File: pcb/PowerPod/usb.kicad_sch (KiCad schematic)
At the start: 8 parts, among them IC2 FUSB302MPX, J1 GT-USB-7010, U1 SRV05-4

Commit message: finished layout
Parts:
- added C14, C24, C25: 100n, Capacitor_SMD:C_0402_1005Metric, symbol Capacitor_JLC:100n
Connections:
- net +3V3: now also C14.2, C24.2, C25.2
- net GND: now also C14.1, C24.1, C25.1
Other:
- moved on the sheet: C6

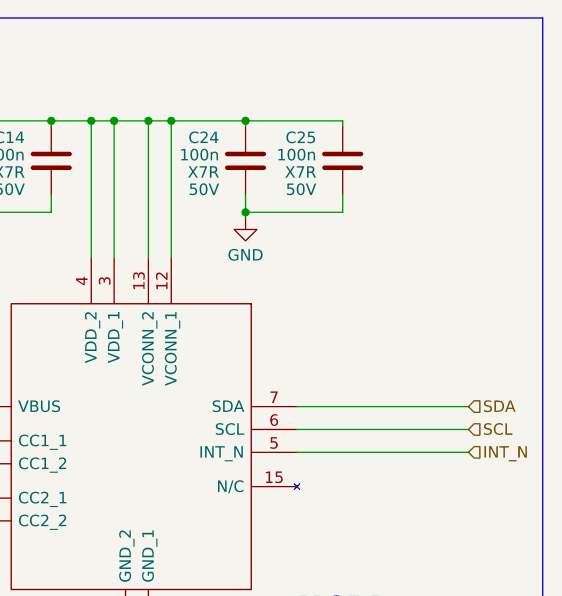
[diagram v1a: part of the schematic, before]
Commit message: changed gpio pins
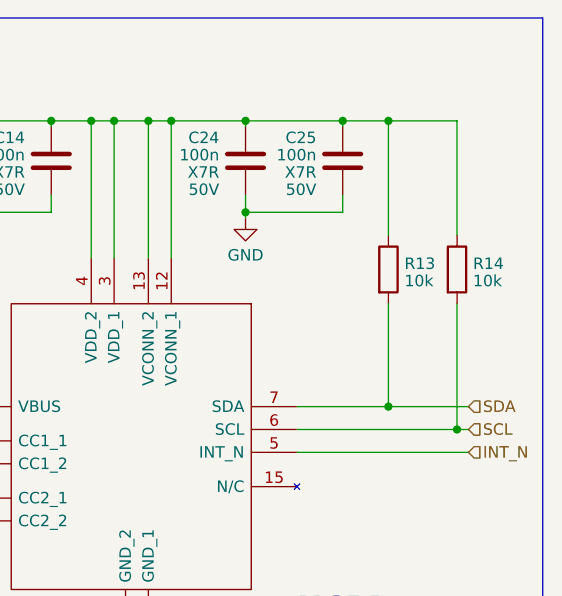
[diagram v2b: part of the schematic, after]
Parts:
- added R13, R14: 10k, Resistor_SMD:R_0402_1005Metric, symbol Resistor_JLC:10k
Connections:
- net +3V3: now also R13.1, R14.1
- net SCL: now also R14.2
- net SDA: now also R13.2
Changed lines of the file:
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@@
   (junction (at 279.4 71.12) (diameter 0) (color 0 0 0 0)
   )
+  (junction (at 335.28 105.41) (diameter 0) (color 0 0 0 0)
+  )
   (junction (at 167.005 102.87) (diameter 0) (color 0 0 0 0)
   )
@@
   (junction (at 126.365 174.625) (diameter 0) (color 0 0 0 0)
   )
+  (junction (at 327.66 102.87) (diameter 0) (color 0 0 0 0)
+  )
   (junction (at 146.685 153.035) (diameter 0) (color 0 0 0 0)
   )
   (junction (at 294.64 71.12) (diameter 0) (color 0 0 0 0)
   )
+  (junction (at 322.58 71.12) (diameter 0) (color 0 0 0 0)
+  )
   (junction (at 256.54 180.34) (diameter 0) (color 0 0 0 0)
+  )
+  (junction (at 327.66 71.12) (diameter 0) (color 0 0 0 0)
   )
   (junction (at 303.53 71.12) (diameter 0) (color 0 0 0 0)
@@
   (no_connect (at 144.145 163.195))
   (no_connect (at 144.145 165.735))
+  (wire (pts (xy 327.66 102.87) (xy 336.55 102.87))
+    (stroke (width 0) (type default))
+  )
   (wire (pts (xy 167.005 102.87) (xy 167.005 137.795))
     (stroke (width 0) (type default))
@@
     (stroke (width 0) (type default))
   )
+  (wire (pts (xy 335.28 71.12) (xy 335.28 83.82))
+    (stroke (width 0) (type default))
+  )
   (wire (pts (xy 182.88 140.335) (xy 182.88 142.875))
     (stroke (width 0) (type default))
@@
     (stroke (width 0) (type default))
   )
+  (wire (pts (xy 335.28 91.44) (xy 335.28 105.41))
+    (stroke (width 0) (type default))
+  )
   (wire (pts (xy 290.195 71.12) (xy 294.64 71.12))
     (stroke (width 0) (type default))
@@
     (stroke (width 0) (type default))
   )
+  (wire (pts (xy 327.66 91.44) (xy 327.66 102.87))
+    (stroke (width 0) (type default))
+  )
   (wire (pts (xy 197.485 135.255) (xy 227.965 135.255))
     (stroke (width 0) (type default))
@@
     (stroke (width 0) (type default))
   )
+  (wire (pts (xy 335.28 105.41) (xy 336.55 105.41))
+    (stroke (width 0) (type default))
+  )
   (wire (pts (xy 300.99 130.81) (xy 300.99 132.715))
     (stroke (width 0) (type default))
@@
     (stroke (width 0) (type default))
   )
-  (wire (pts (xy 317.5 105.41) (xy 336.55 105.41))
+  (wire (pts (xy 317.5 105.41) (xy 335.28 105.41))
     (stroke (width 0) (type default))
   )
@@
     (stroke (width 0) (type default))
   )
+  (wire (pts (xy 327.66 71.12) (xy 327.66 83.82))
+    (stroke (width 0) (type default))
+  )
   (wire (pts (xy 121.285 175.895) (xy 126.365 175.895))
     (stroke (width 0) (type default))
@@
     (stroke (width 0) (type default))
   )
-  (wire (pts (xy 317.5 102.87) (xy 336.55 102.87))
+  (wire (pts (xy 317.5 102.87) (xy 327.66 102.87))
     (stroke (width 0) (type default))
   )
@@
     (stroke (width 0) (type default))
   )
+  (wire (pts (xy 322.58 71.12) (xy 327.66 71.12))
+    (stroke (width 0) (type default))
+  )
   (wire (pts (xy 126.365 173.355) (xy 126.365 174.625))
+    (stroke (width 0) (type default))
+  )
+  (wire (pts (xy 327.66 71.12) (xy 335.28 71.12))
     (stroke (width 0) (type default))
   )
@@
     )
   )
+  (symbol (lib_id "Resistor_JLC:10k") (at 327.66 87.63 0) (unit 1)
+    (in_bom yes) (on_board yes) (dnp no) (fields_autoplaced)
+    (property "Reference" "R13" (at 329.438 86.9863 0)
+      (effects (font (size 1.27 1.27)) (justify left))
+    )
+    (property "Value" "10k" (at 329.438 88.9073 0)
+      (effects (font (size 1.27 1.27)) (justify left))
+    )
+    (property "Footprint" "Resistor_SMD:R_0402_1005Metric" (at 325.882 87.63 90)
+      (effects (font (size 1.27 1.27)) hide)
+    )
+    (property "Datasheet" "~" (at 327.66 87.63 0)
+      (effects (font (size 1.27 1.27)) hide)
+    )
+    (property "LCSC" "C25744" (at 327.66 87.63 0)
+      (effects (font (size 1.27 1.27)) hide)
+    )
+    (pin "1")
+    (pin "2")
+    (instances
+      (project "PowerPod"
+        (path "/e63e39d7-6ac0-4ffd-8aa3-1841a4541b55/dc0e84e0-adcd-432b-9bb1-644eba2790b5"
+          (reference "R13") (unit 1)
+        )
+        (path "/e63e39d7-6ac0-4ffd-8aa3-1841a4541b55/6cfbe2b3-9694-4186-b330-88c2d820dbd8"
+          (reference "R13") (unit 1)
+        )
+      )
+    )
+  )
   (symbol (lib_id "power:GND") (at 279.4 81.915 0) (unit 1)
     (in_bom yes) (on_board yes) (dnp no) (fields_autoplaced)
@@
         )
       )
+    )
+  )
+  (symbol (lib_id "Resistor_JLC:10k") (at 335.28 87.63 0) (unit 1)
+    (in_bom yes) (on_board yes) (dnp no) (fields_autoplaced)
+    (property "Reference" "R14" (at 337.058 86.9863 0)
+      (effects (font (size 1.27 1.27)) (justify left))
+    )
+    (property "Value" "10k" (at 337.058 88.9073 0)
+      (effects (font (size 1.27 1.27)) (justify left))
+    )
+    (property "Footprint" "Resistor_SMD:R_0402_1005Metric" (at 333.502 87.63 90)
+      (effects (font (size 1.27 1.27)) hide)
+    )
+    (property "Datasheet" "~" (at 335.28 87.63 0)
+      (effects (font (size 1.27 1.27)) hide)
+    )
+    (property "LCSC" "C25744" (at 335.28 87.63 0)
+      (effects (font (size 1.27 1.27)) hide)
+    )
+    (pin "1")
+    (pin "2")
+    (instances
+      (project "PowerPod"
+        (path "/e63e39d7-6ac0-4ffd-8aa3-1841a4541b55/dc0e84e0-adcd-432b-9bb1-644eba2790b5"
+          (reference "R14") (unit 1)
+        )
+        (path "/e63e39d7-6ac0-4ffd-8aa3-1841a4541b55/6cfbe2b3-9694-4186-b330-88c2d820dbd8"
+          (reference "R14") (unit 1)
+        )
+      )
